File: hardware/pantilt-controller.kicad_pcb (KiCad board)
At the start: 4 copper layers, 52.3 x 93.2 mm, 83 parts, among them J1 Conn_01x22_Socket, J17 Motor_Slide, J18 Motor_Pan, J19 Motor_Tilt, J2 Conn_01x22_Socket, J20 TCA9548A_Mux, J21 AS5600_Pan, J22 AS5600_Tilt, J23 OLED, J24 TCA9548A_Mux, J26 Limit_Min, J27 Limit_Max, J28 Motor_Aux, J29 Enc_Slide, J3 MUX_2, J30 Enc_Pan, J31 Enc_Tilt, J32 Enc_Aux, J33 Btn_SetKeyframe, J34 Btn_ClearKeyframe, J35 Btn_PlayPause, J36 Btn_Reset, J37 5V_In, J38 24V_In, J4 MUX_3, J41 Aux_Max, J5 MUX_4, J6 MUX_5, J7 MUX_6, J8 MUX_7, U1 tmc2209, U2 tmc2209, U3 tmc2209, U4 tmc2209

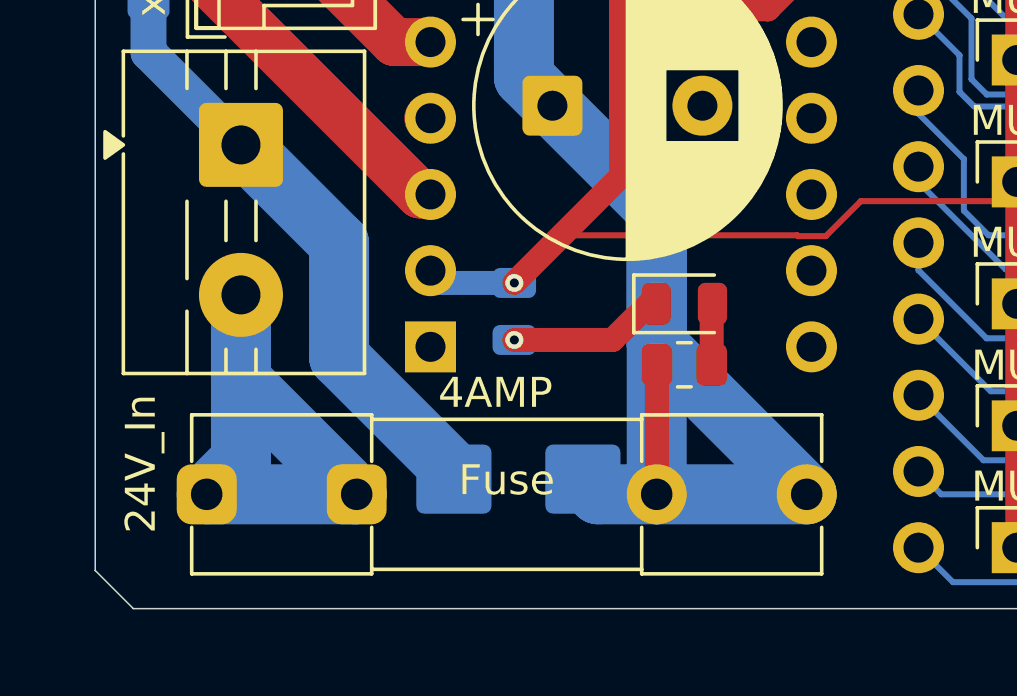
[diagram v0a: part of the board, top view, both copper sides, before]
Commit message: correcting fuse holder
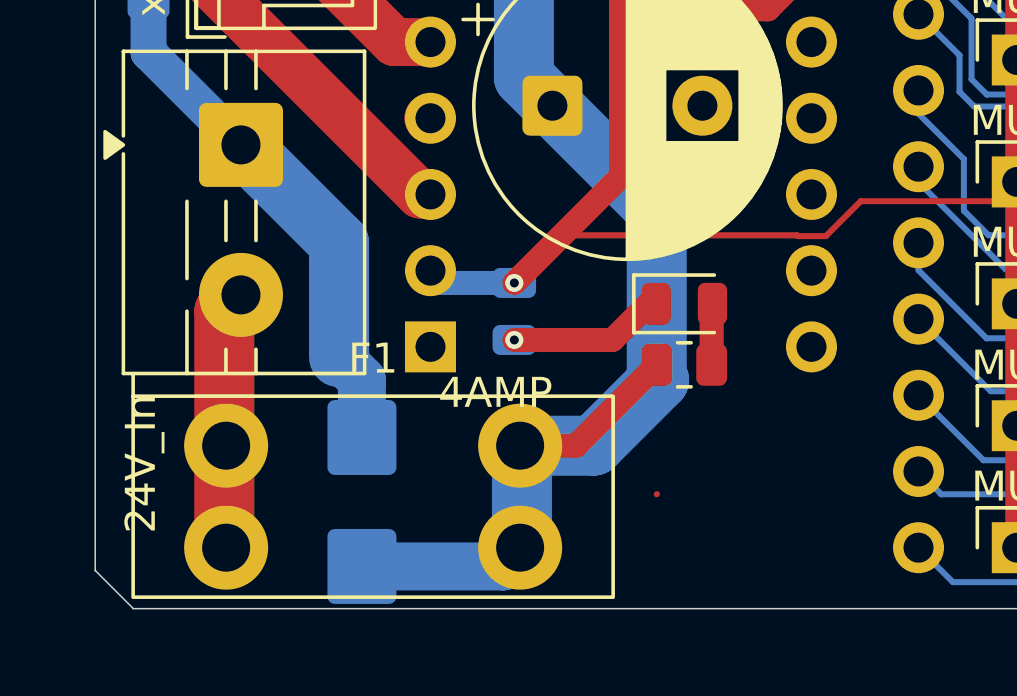
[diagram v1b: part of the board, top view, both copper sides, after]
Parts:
- F1: value Fuse -> 4A; footprint Fuse:Fuseholder_Clip-5x20mm_Littelfuse_111_Inline_P20.00x5.00mm_D1.05mm_Horizontal -> PanTilt:Fuseholder_Blade_Mini_XFCN_XF-508P-B-B
- moved F1 5.55 mm to (96.4, 107.3)
- moved D1 5.27 mm to (96.0, 107.4), turned to -90 degrees
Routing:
- net Net-(J38-Pin_2): track 20.4 -> 8.66 mm
- net +24V: track 179.1 -> 172.2 mm
- net GND: track 45.4 -> 42.7 mm

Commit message: updates
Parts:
- added REF**: MountingHole_3.2mm_M3, MountingHole:MountingHole_3.2mm_M3, F.Cu at (91.4, 106.7)
- moved D1 9.43 mm to (104.4, 103.1)
- moved F1 8.26 mm to (104.6, 107.4)
- moved J28 3.84 mm to (92.4, 85.3)
- moved J38 1.05 mm to (91.7, 94.5)
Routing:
- net +24V: track 172.2 -> 184.5 mm
- net GND: track 42.7 -> 51.8 mm
- net Net-(J38-Pin_2): track 8.66 -> 14.0 mm
- net AUX_M1A: track 8.55 -> 12.1 mm
- net AUX_M2A: track 11.3 -> 14.7 mm
- net AUX_M1B: track 15.4 -> 18.5 mm
- net AUX_M2B: track 11.3 -> 14.0 mm
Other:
- board text added: "tmc2209"
- board text removed: "4AMP"

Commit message: fixing the errors cluad found
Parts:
- moved F1 0.51 mm to (104.6, 106.9)
- moved J17 0.19 mm to (92.5, 71.6)
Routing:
- net AUX_M1B: track 18.5 -> 19.6 mm
- net +24V: track 184.5 -> 185.1 mm
- net AUX_M2B: track 14.0 -> 14.5 mm

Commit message: fixes
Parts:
- moved D1 0.25 mm to (104.4, 103.4)
- moved R31 0.25 mm to (106.8, 102.6)
- moved LED1 0.25 mm to (106.8, 100.6)
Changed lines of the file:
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@@
 	(footprint "Resistor_SMD:R_0805_2012Metric"
 		(layer "F.Cu")
-		(at 106.7585 102.87 180)
+		(at 106.7585 102.616 180)
 		(descr "Resistor SMD 0805 (2012 Metric), square (rectangular) end terminal, IPC-7351 nominal, (Body size source: IPC-SM-782 page 72, https://www.pcb-3d.com/wordpress/wp-content/uploads/ipc-sm-782a_amendment_1_and_2.pdf)")
 		(tags "resistor")
@@
 		)
 		(fp_text user "${REFERENCE}"
-			(at 0 0 0)
-			(layer "F.Fab")
+			(at 0.254 1.27 0)
+			(layer "F.SilkS")
 			(effects
 				(font
@@
 	(footprint "LED_SMD:LED_0805_2012Metric"
 		(layer "F.Cu")
-		(at 106.7585 100.838)
+		(at 106.7585 100.584)
 		(descr "LED SMD 0805 (2012 Metric), square (rectangular) end terminal, IPC-7351 nominal, (Body size source: https://docs.google.com/spreadsheets/d/1BsfQQcO9C6DZCsRaXUlFlo91Tg2WpOkGARC1WS5S8t0/edit?usp=sharing)")
 		(tags "LED")
@@
 	(footprint "Diode_SMD:D_SMB"
 		(layer "B.Cu")
-		(at 104.394 103.124 -90)
+		(at 104.394 103.378 -90)
 		(descr "Diode SMB (DO-214AA)")
 		(tags "Diode SMB (DO-214AA)")
@@
 	)
 	(segment
-		(start 137.668 76.7865)
-		(end 137.668 73.66)
+		(start 105.821 100.584)
+		(end 104.363 102.042)
 		(width 0.8)
 		(layer "F.Cu")
@@
 	)
 	(segment
-		(start 105.821 100.584)
-		(end 104.363 102.042)
+		(start 137.668 76.7865)
+		(end 137.668 73.66)
 		(width 0.8)
 		(layer "F.Cu")
@@
 	)
 	(segment
-		(start 103.096094 102.271906)
-		(end 104.394 100.974)
-		(width 2)
-		(layer "B.Cu")
-		(net "GND")
-	)
-	(segment
 		(start 132.2415 86.9425)
 		(end 133.35 85.834)
@@
 	)
 	(segment
+		(start 103.096094 102.271906)
+		(end 104.14 101.228)
+		(width 2)
+		(layer "B.Cu")
+		(net "GND")
+	)
+	(segment
 		(start 88.9 92.4595)
 		(end 91.9805 95.54)
@@
 	)
 	(segment
-		(start 98.298 102.271906)
-		(end 103.096094 102.271906)
+		(start 104.14 101.228)
+		(end 104.394 101.228)
 		(width 2)
 		(layer "B.Cu")
@@
 	)
 	(segment
+		(start 98.298 102.271906)
+		(end 103.096094 102.271906)
+		(width 2)
+		(layer "B.Cu")
+		(net "GND")
+	)
+	(segment
 		(start 98.527906 102.042)
 		(end 98.298 102.271906)
@@
 	)
 	(segment
-		(start 105.846 104.019898)
-		(end 105.846 102.87)
+		(start 107.568102 105.742)
+		(end 105.846 104.019898)
 		(width 0.8)
 		(layer "F.Cu")
@@
 	)
 	(segment
-		(start 107.568102 105.742)
-		(end 105.846 104.019898)
+		(start 105.846 104.019898)
+		(end 105.846 102.616)
 		(width 0.8)
 		(layer "F.Cu")
@@
 	)
 	(segment
-		(start 105.68 105.274)
-		(end 109.04 108.634)
+		(start 98.298 20.066)
+		(end 100.97 20.066)
 		(width 2)
 		(layer "B.Cu")
@@
 	)
 	(segment
-		(start 98.298 20.066)
-		(end 100.97 20.066)
+		(start 105.886 72.486651)
+		(end 102.233349 68.834)
 		(width 2)
 		(layer "B.Cu")
@@
 	)
 	(segment
-		(start 105.886 72.486651)
-		(end 102.233349 68.834)
+		(start 102.233349 68.834)
+		(end 102.233349 66.075254)
 		(width 2)
 		(layer "B.Cu")
@@
 	)
 	(segment
-		(start 98.969905 63.155905)
-		(end 98.298 63.155905)
+		(start 102.233349 66.075254)
+		(end 99.314 63.155905)
 		(width 2)
 		(layer "B.Cu")
@@
 	)
 	(segment
-		(start 102.233349 66.419349)
-		(end 98.969905 63.155905)
+		(start 109.548 105.742)
+		(end 104.862 105.742)
 		(width 2)
 		(layer "B.Cu")
@@
 	)
 	(segment
-		(start 108.204 104.398)
-		(end 108.204 100.076)
-		(width 2)
-		(layer "B.Cu")
-		(net "+24V")
-	)
-	(segment
 		(start 102.233349 47.498)
 		(end 101.412 46.676651)
@@
 	)
 	(segment
+		(start 109.04 108.634)
+		(end 109.548 108.634)
+		(width 2)
+		(layer "B.Cu")
+		(net "+24V")
+	)
+	(segment
 		(start 101.412 84.745906)
 		(end 101.412 82.992)
@@
 	)
 	(segment
-		(start 109.548 105.742)
-		(end 108.204 104.398)
+		(start 100.97 20.066)
+		(end 100.97 24.390651)
 		(width 2)
 		(layer "B.Cu")
@@
 	)
 	(segment
-		(start 100.97 20.066)
-		(end 100.97 24.390651)
+		(start 105.934 105.528)
+		(end 109.04 108.634)
+		(width 2)
+		(layer "B.Cu")
+		(net "+24V")
+	)
+	(segment
+		(start 108.204 100.076)
+		(end 108.204 104.398)
 		(width 2)
 		(layer "B.Cu")
@@
 	)
 	(segment
+		(start 102.362 94.234)
+		(end 108.204 100.076)
+		(width 2)
+		(layer "B.Cu")
+		(net "+24V")
+	)
+	(segment
 		(start 98.388095 41.656)
 		(end 98.298 41.565905)
@@
 	)
 	(segment
-		(start 104.394 105.274)
-		(end 105.68 105.274)
+		(start 98.298 63.155905)
+		(end 100.431557 63.155905)
 		(width 2)
 		(layer "B.Cu")
@@
 	)
 	(segment
-		(start 109.04 108.634)
-		(end 109.548 108.634)
+		(start 99.314 63.155905)
+		(end 98.298 63.155905)
 		(width 2)
 		(layer "B.Cu")
@@
 	)
 	(segment
-		(start 104.862 105.742)
-		(end 104.394 105.274)
-		(width 2)
-		(layer "B.Cu")
-		(net "+24V")
-	)
-	(segment
-		(start 109.548 105.742)
-		(end 104.862 105.742)
+		(start 101.224 63.246)
+		(end 101.224 67.824651)
 		(width 2)
 		(layer "B.Cu")
@@
 	)
 	(segment
-		(start 101.224 63.246)
-		(end 101.224 67.824651)
+		(start 99.035905 41.565905)
+		(end 102.233349 44.763349)
 		(width 2)
 		(layer "B.Cu")
@@
 	)
 	(segment
-		(start 99.035905 41.565905)
-		(end 102.233349 44.763349)
+		(start 103.886 59.701462)
+		(end 101.224 62.363462)
 		(width 2)
 		(layer "B.Cu")
@@
 	)
 	(segment
-		(start 102.233349 68.834)
-		(end 102.233349 66.419349)
+		(start 101.412 46.676651)
+		(end 101.412 41.656)
 		(width 2)
 		(layer "B.Cu")
@@
 	)
 	(segment
-		(start 103.886 59.701462)
-		(end 101.224 62.363462)
+		(start 101.412 84.745906)
+		(end 98.552 84.745906)
 		(width 2)
 		(layer "B.Cu")
@@
 	)
 	(segment
-		(start 98.298 63.155905)
-		(end 99.095254 63.155905)
+		(start 101.979349 22.545268)
+		(end 99.500081 20.066)
 		(width 2)
 		(layer "B.Cu")
@@
 	)
 	(segment
-		(start 101.412 46.676651)
-		(end 101.412 41.656)
+		(start 103.886 80.518)
+		(end 105.886 78.518)
 		(width 2)
 		(layer "B.Cu")
@@
 	)
 	(segment
-		(start 101.412 84.745906)
-		(end 98.552 84.745906)
+		(start 104.648 105.528)
+		(end 104.394 105.528)
 		(width 2)
 		(layer "B.Cu")
@@
 	)
 	(segment
-		(start 101.979349 22.545268)
-		(end 99.500081 20.066)
+		(start 100.431557 63.155905)
+		(end 101.224 62.363462)
 		(width 2)
 		(layer "B.Cu")
@@
 	)
 	(segment
-		(start 103.886 80.518)
-		(end 105.886 78.518)
+		(start 104.862 105.742)
+		(end 104.648 105.528)
 		(width 2)
 		(layer "B.Cu")
@@
 	)
 	(segment
+		(start 108.204 104.398)
+		(end 109.548 105.742)
+		(width 2)
+		(layer "B.Cu")
+		(net "+24V")
+	)
+	(segment
 		(start 96.648 82.841906)
 		(end 96.648 78.980963)
@@
 	)
 	(segment
-		(start 108.204 100.076)
-		(end 102.362 94.234)
-		(width 2)
-		(layer "B.Cu")
-		(net "+24V")
-	)
-	(segment
 		(start 99.912094 84.491906)
 		(end 98.298 84.491906)
@@
 	)
 	(segment
-		(start 101.412 41.656)
-		(end 98.388095 41.656)
+		(start 104.394 105.528)
+		(end 105.934 105.528)
 		(width 2)
 		(layer "B.Cu")
@@
 	)
 	(segment
-		(start 101.224 63.246)
-		(end 98.388095 63.246)
+		(start 101.412 41.656)
+		(end 98.388095 41.656)
 		(width 2)
 		(layer "B.Cu")
@@
 		(start 107.671 100.609)
 		(end 107.696 100.584)
-		(width 0.2)
+		(width 0.8)
 		(layer "F.Cu")
 		(net "Net-(LED1-A)")
 	)
 	(segment
-		(start 107.671 102.6)
+		(start 107.671 102.616)
 		(end 107.671 100.609)
 		(width 0.8)

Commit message: fixing f1
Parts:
- moved F1 0.25 mm to (104.6, 107.2)
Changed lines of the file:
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@@
 	(footprint "PanTilt:Fuseholder_Blade_Mini_XFCN_XF-508P-B-B"
 		(layer "F.Cu")
-		(at 104.648 106.934)
+		(at 104.648 107.188)
 		(descr "XFCN XF-508P-B-B MINI (ATM) automotive blade fuse holder, THT. Hole grid 9.80 x 3.40mm, 4x 1.6mm min round. Body 16.00 x 6.70mm, 7.35mm tall. 500V, 15-30A. LCSC C19727305.")
 		(tags "fuse holder blade mini ATM automotive XFCN")
@@
 	)
 	(segment
+		(start 109.294 108.634)
+		(end 109.548 108.888)
+		(width 2)
+		(layer "B.Cu")
+		(net "+24V")
+	)
+	(segment
 		(start 102.233349 47.498)
 		(end 101.412 46.676651)
@@
 	)
 	(segment
-		(start 109.04 108.634)
-		(end 109.548 108.634)
-		(width 2)
-		(layer "B.Cu")
-		(net "+24V")
-	)
-	(segment
 		(start 101.412 84.745906)
 		(end 101.412 82.992)
@@
 	)
 	(segment
-		(start 105.934 105.528)
-		(end 109.04 108.634)
+		(start 108.204 100.076)
+		(end 108.204 104.398)
 		(width 2)
 		(layer "B.Cu")
@@
 	)
 	(segment
-		(start 108.204 100.076)
-		(end 108.204 104.398)
+		(start 101.979349 25.4)
+		(end 104.062 27.482651)
 		(width 2)
 		(layer "B.Cu")
@@
 	)
 	(segment
-		(start 101.979349 25.4)
-		(end 104.062 27.482651)
+		(start 105.934 105.528)
+		(end 109.04 108.634)
 		(width 2)
 		(layer "B.Cu")
@@
 	)
 	(segment
+		(start 104.394 105.528)
+		(end 105.934 105.528)
+		(width 2)
+		(layer "B.Cu")
+		(net "+24V")
+	)
+	(segment
 		(start 98.298 84.491906)
 		(end 96.648 82.841906)
@@
 	)
 	(segment
-		(start 109.548 108.634)
-		(end 109.548 105.234)
-		(width 2)
-		(layer "B.Cu")
-		(net "+24V")
-	)
-	(segment
 		(start 99.314 63.155905)
 		(end 98.298 63.155905)
@@
 	)
 	(segment
+		(start 109.04 108.634)
+		(end 109.294 108.634)
+		(width 2)
+		(layer "B.Cu")
+		(net "+24V")
+	)
+	(segment
 		(start 101.979349 25.4)
 		(end 101.979349 22.545268)
@@
 	)
 	(segment
+		(start 109.548 108.888)
+		(end 109.548 105.488)
+		(width 2)
+		(layer "B.Cu")
+		(net "+24V")
+	)
+	(segment
 		(start 102.233349 44.763349)
 		(end 102.233349 47.498)
@@
 	)
 	(segment
-		(start 104.394 105.528)
-		(end 105.934 105.528)
-		(width 2)
-		(layer "B.Cu")
-		(net "+24V")
-	)
-	(segment
 		(start 101.412 41.656)
 		(end 98.388095 41.656)
@@
 	)
 	(segment
-		(start 99.748 105.234)
-		(end 99.748 108.634)
-		(width 2)
-		(layer "F.Cu")
-		(net "Net-(J38-Pin_2)")
-	)
-	(segment
 		(start 91.7265 99.524)
-		(end 97.9445 105.742)
+		(end 97.6905 105.488)
 		(width 2)
 		(layer "F.Cu")
@@
 	)
 	(segment
-		(start 97.9445 105.742)
-		(end 99.24 105.742)
+		(start 99.748 105.488)
+		(end 99.748 108.888)
 		(width 2)
 		(layer "F.Cu")
@@
 	)
 	(segment
-		(start 99.24 105.742)
-		(end 99.748 105.234)
+		(start 97.6905 105.488)
+		(end 99.748 105.488)
 		(width 2)
 		(layer "F.Cu")
